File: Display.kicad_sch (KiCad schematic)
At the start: 31 parts, among them J14 LCD_TP_I2C, J15 LCD_SPI, J2 TFT_LCD, U3 MT9284, U5 TPS61169

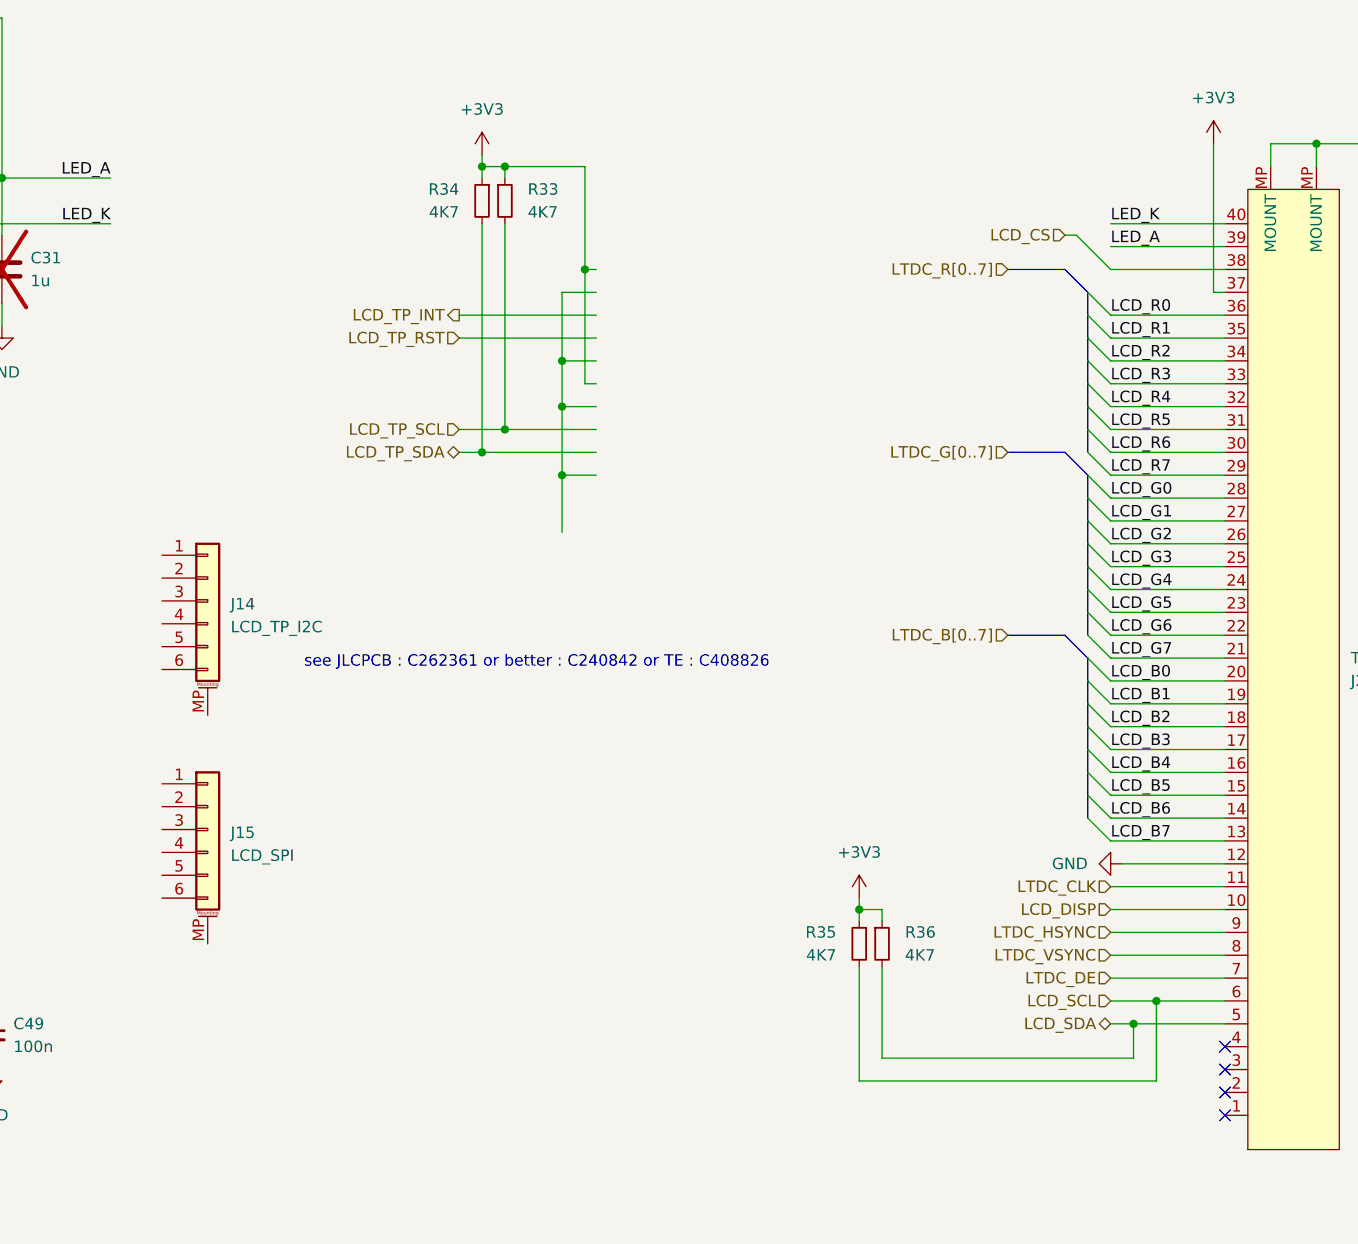
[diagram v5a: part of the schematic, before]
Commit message: Changes: USB C to midmount, CR1220 socket, flip MCU to shorten the LCD traces
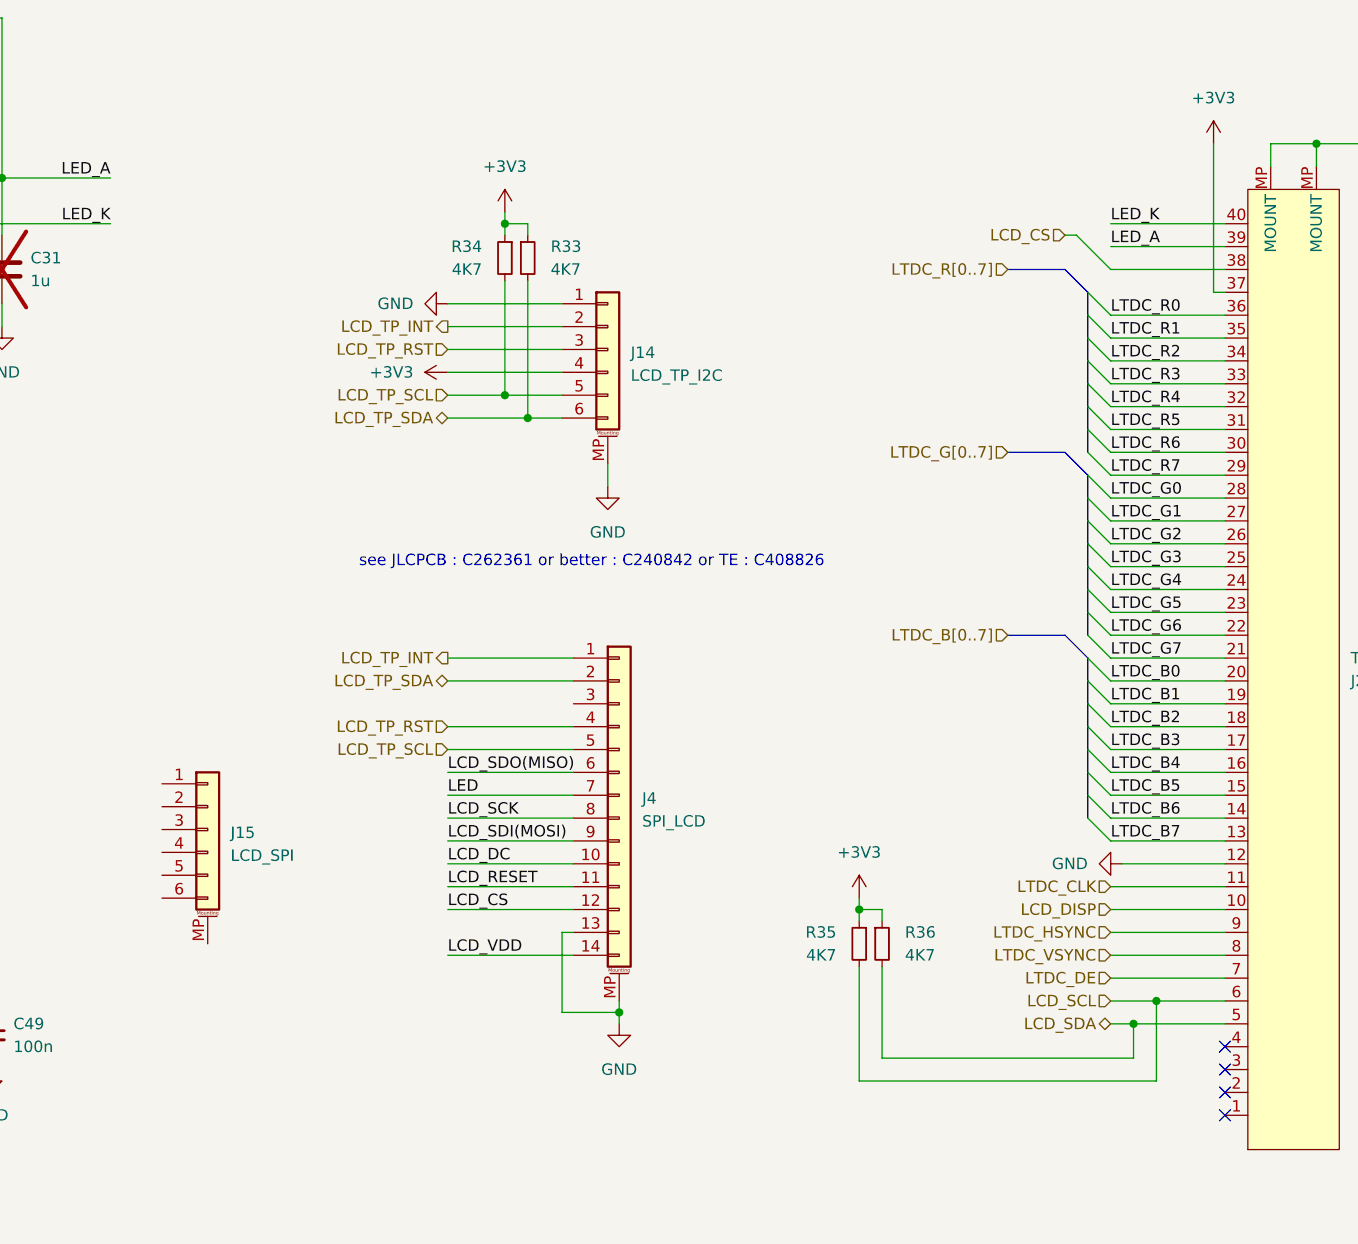
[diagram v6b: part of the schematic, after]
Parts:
- added J4: SPI_LCD, Connector_FFC-FPC:TE_1-84953-4_1x14-1MP_P1.0mm_Horizontal, symbol Connector_Generic_MountingPin:Conn_01x14_MountingPin
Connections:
- net +3V3: now also J14.4 (Pin_4)
- net GND: now also J14.1 (Pin_1), J14.MP (MountPin), J4.13 (Pin_13), J4.MP (MountPin)
- net LCD_CS: now also J4.12 (Pin_12)
- net LCD_TP_INT: now also J14.2 (Pin_2), J4.1 (Pin_1)
- net LCD_TP_RST: now also J14.3 (Pin_3), J4.4 (Pin_4)
- net LCD_TP_SCL: now also J14.5 (Pin_5), R34.2, J4.5 (Pin_5); no longer R33.2
- net LCD_TP_SDA: now also J14.6 (Pin_6), R33.2, J4.2 (Pin_2); no longer R34.2
- net LCD_B0 renamed LTDC_B0
- net LCD_B1 renamed LTDC_B1
- net LCD_B2 renamed LTDC_B2
- net LCD_B3 renamed LTDC_B3
- net LCD_B4 renamed LTDC_B4
- net LCD_B5 renamed LTDC_B5
- net LCD_B6 renamed LTDC_B6
- net LCD_B7 renamed LTDC_B7
- net LCD_G0 renamed LTDC_G0
- net LCD_G1 renamed LTDC_G1
- net LCD_G2 renamed LTDC_G2
- net LCD_G3 renamed LTDC_G3
- net LCD_G4 renamed LTDC_G4
- net LCD_G5 renamed LTDC_G5
- net LCD_G6 renamed LTDC_G6
- net LCD_G7 renamed LTDC_G7
- net LCD_R0 renamed LTDC_R0
- net LCD_R1 renamed LTDC_R1
- net LCD_R2 renamed LTDC_R2
- net LCD_R3 renamed LTDC_R3
- net LCD_R4 renamed LTDC_R4
- net LCD_R5 renamed LTDC_R5
- net LCD_R6 renamed LTDC_R6
- net LCD_R7 renamed LTDC_R7
- new net LCD_DC: J4.10 (Pin_10)
- new net LCD_RESET: J4.11 (Pin_11)
- new net LCD_SCK: J4.8 (Pin_8)
- new net LCD_SDI(MOSI): J4.9 (Pin_9)
- new net LCD_SDO(MISO): J4.6 (Pin_6)
- new net LCD_VDD: J4.14 (Pin_14)
- new net LED: J4.7 (Pin_7)
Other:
- moved on the sheet: J14, R33, R34

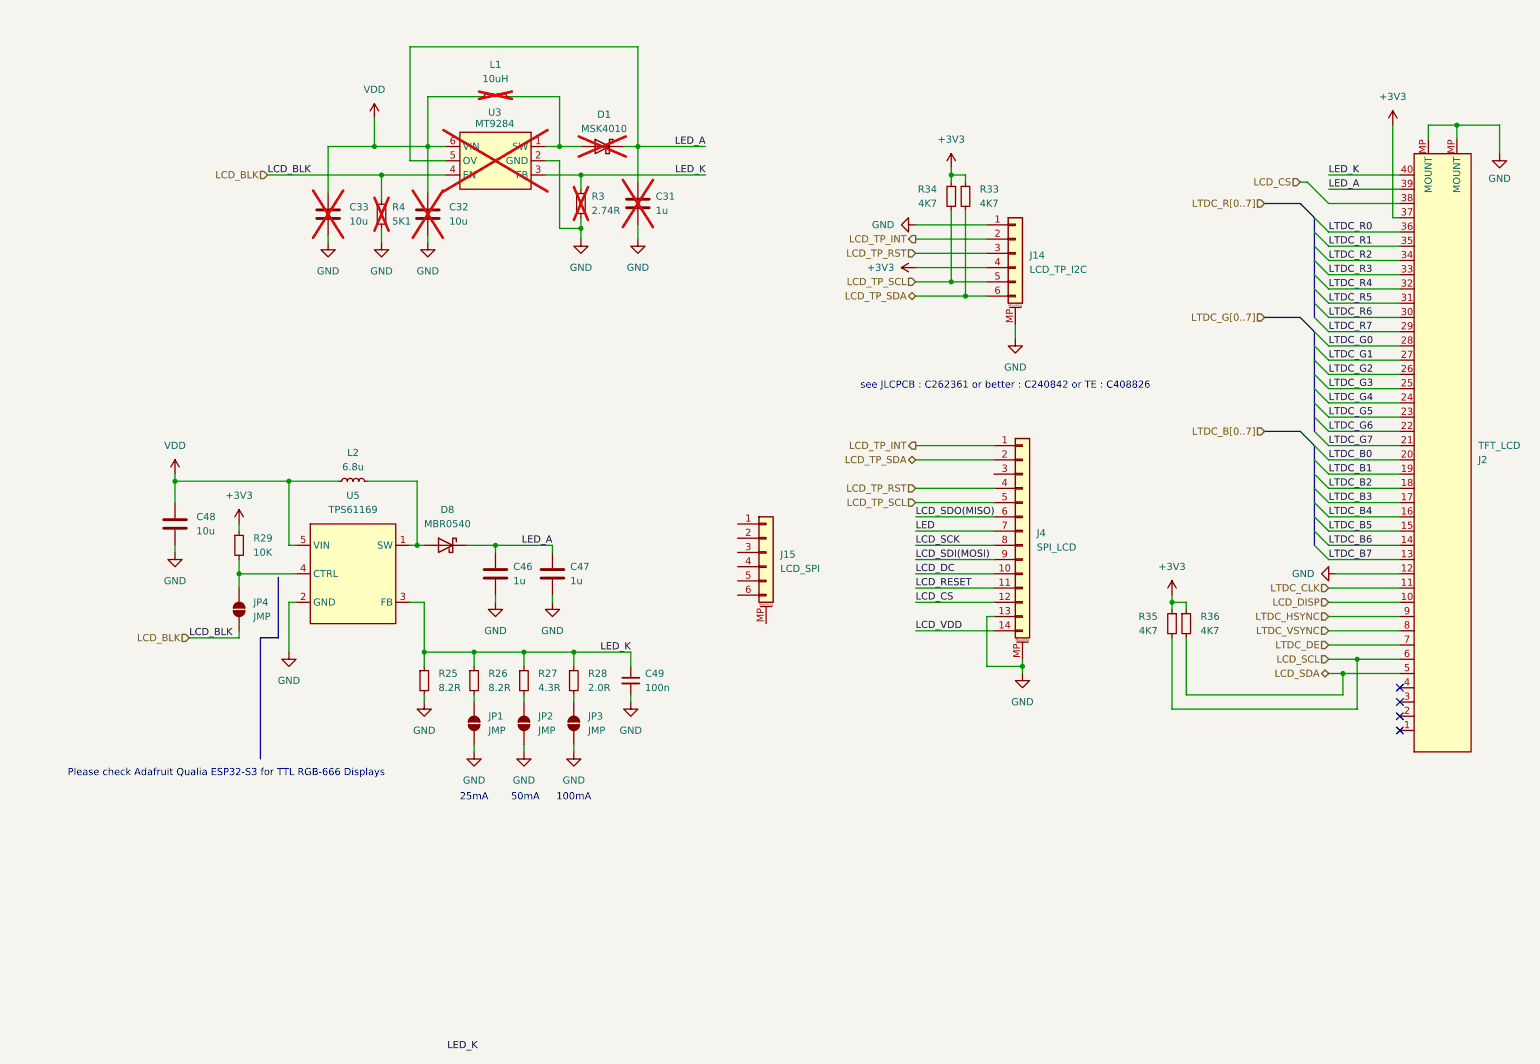
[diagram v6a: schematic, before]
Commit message: Finished SDRAM, LTDC, QSPI, SDMMC, still an error on LTDC B channel
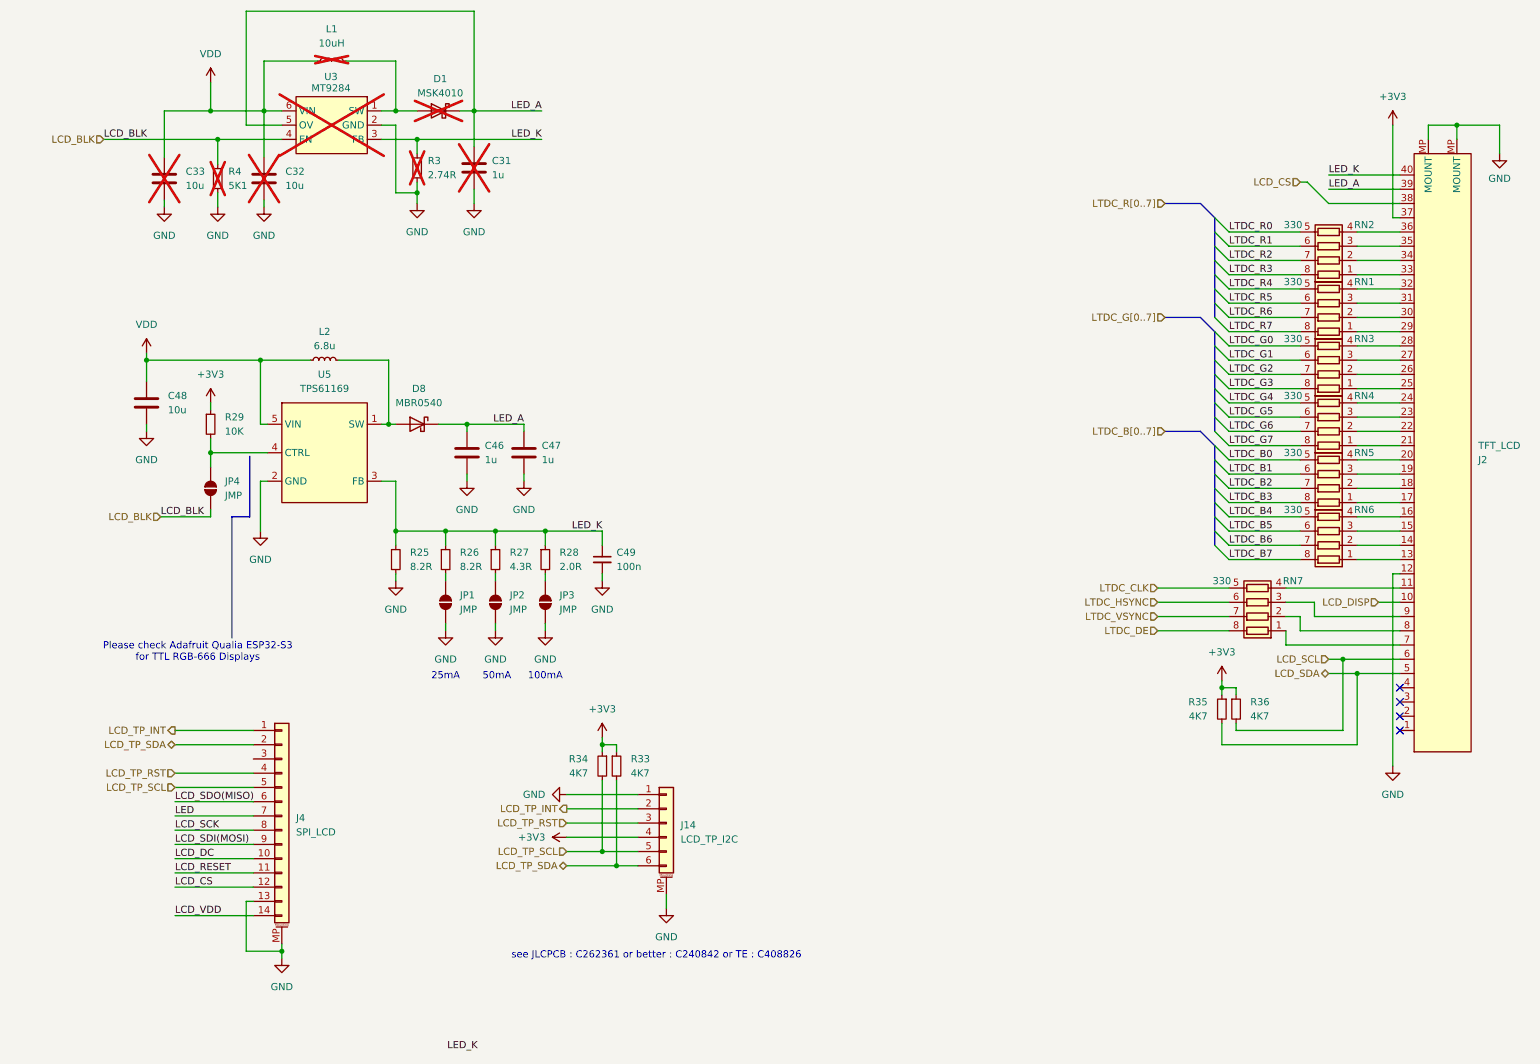
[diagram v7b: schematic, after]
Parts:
- removed J15: LCD_SPI, Connector_FFC-FPC:TE_84952-6_1x06-1MP_P1.0mm_Horizontal, symbol Connector_Generic_MountingPin:Conn_01x06_MountingPin
- added RN1, RN2, RN3, RN4, RN5, RN6, RN7: 330, Resistor_SMD:R_Array_Convex_4x0603, symbol Device:R_Pack04
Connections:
- net LCD_SCL: now also R36.2; no longer R35.2
- net LCD_SDA: now also R35.2; no longer R36.2
- net LTDC_B0: now also RN5.5 (R4.2); no longer J2.20
- net LTDC_B1: now also RN5.6 (R3.2); no longer J2.19
- net LTDC_B2: now also RN5.7 (R2.2); no longer J2.18
- net LTDC_B3: now also RN5.8 (R1.2); no longer J2.17
- net LTDC_B4: now also RN6.5 (R4.2); no longer J2.16
- net LTDC_B5: now also RN6.6 (R3.2); no longer J2.15
- net LTDC_B6: now also RN6.7 (R2.2); no longer J2.14
- net LTDC_B7: now also RN6.8 (R1.2); no longer J2.13
- net LTDC_CLK: now also RN7.5 (R4.2); no longer J2.11
- net LTDC_DE: now also RN7.8 (R1.2); no longer J2.7
- net LTDC_G0: now also RN3.5 (R4.2); no longer J2.28
- net LTDC_G1: now also RN3.6 (R3.2); no longer J2.27
- net LTDC_G2: now also RN3.7 (R2.2); no longer J2.26
- net LTDC_G3: now also RN3.8 (R1.2); no longer J2.25
- net LTDC_G4: now also RN4.5 (R4.2); no longer J2.24
- net LTDC_G5: now also RN4.6 (R3.2); no longer J2.23
- net LTDC_G6: now also RN4.7 (R2.2); no longer J2.22
- net LTDC_G7: now also RN4.8 (R1.2); no longer J2.21
- net LTDC_HSYNC: now also RN7.6 (R3.2); no longer J2.9
- net LTDC_R0: now also RN2.5 (R4.2); no longer J2.36
- net LTDC_R1: now also RN2.6 (R3.2); no longer J2.35
- net LTDC_R2: now also RN2.7 (R2.2); no longer J2.34
- net LTDC_R3: now also RN2.8 (R1.2); no longer J2.33
- net LTDC_R4: now also RN1.5 (R4.2); no longer J2.32
- net LTDC_R5: now also RN1.6 (R3.2); no longer J2.31
- net LTDC_R6: now also RN1.7 (R2.2); no longer J2.30
- net LTDC_R7: now also RN1.8 (R1.2); no longer J2.29
- net LTDC_VSYNC: now also RN7.7 (R2.2); no longer J2.8
- new net: J2.17, RN5.1 (R1.1)
- new net: J2.18, RN5.2 (R2.1)
- new net: J2.19, RN5.3 (R3.1)
- new net: J2.20, RN5.4 (R4.1)
- new net: J2.13, RN6.1 (R1.1)
- new net: J2.14, RN6.2 (R2.1)
- new net: J2.15, RN6.3 (R3.1)
- new net: J2.16, RN6.4 (R4.1)
- new net: J2.25, RN3.1 (R1.1)
- new net: J2.26, RN3.2 (R2.1)
- new net: J2.27, RN3.3 (R3.1)
- new net: J2.28, RN3.4 (R4.1)
- new net: J2.21, RN4.1 (R1.1)
- new net: J2.22, RN4.2 (R2.1)
- new net: J2.23, RN4.3 (R3.1)
- new net: J2.24, RN4.4 (R4.1)
- new net: J2.33, RN2.1 (R1.1)
- new net: J2.34, RN2.2 (R2.1)
- new net: J2.35, RN2.3 (R3.1)
- new net: J2.36, RN2.4 (R4.1)
- new net: J2.29, RN1.1 (R1.1)
- new net: J2.30, RN1.2 (R2.1)
- new net: J2.31, RN1.3 (R3.1)
- new net: J2.32, RN1.4 (R4.1)
- new net: J2.11, RN7.4 (R4.1)
- new net: J2.7, RN7.1 (R1.1)
- new net: J2.8, RN7.2 (R2.1)
- new net: J2.9, RN7.3 (R3.1)
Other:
- moved on the sheet: C31, C32, C33, C46, C47, C48, C49, D1, D8, J14, J4, JP1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

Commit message: Finished SDRAM, QSPI, SDMMC, LTDC, TP, EEPROM, USB, debug (need to verify on UART)
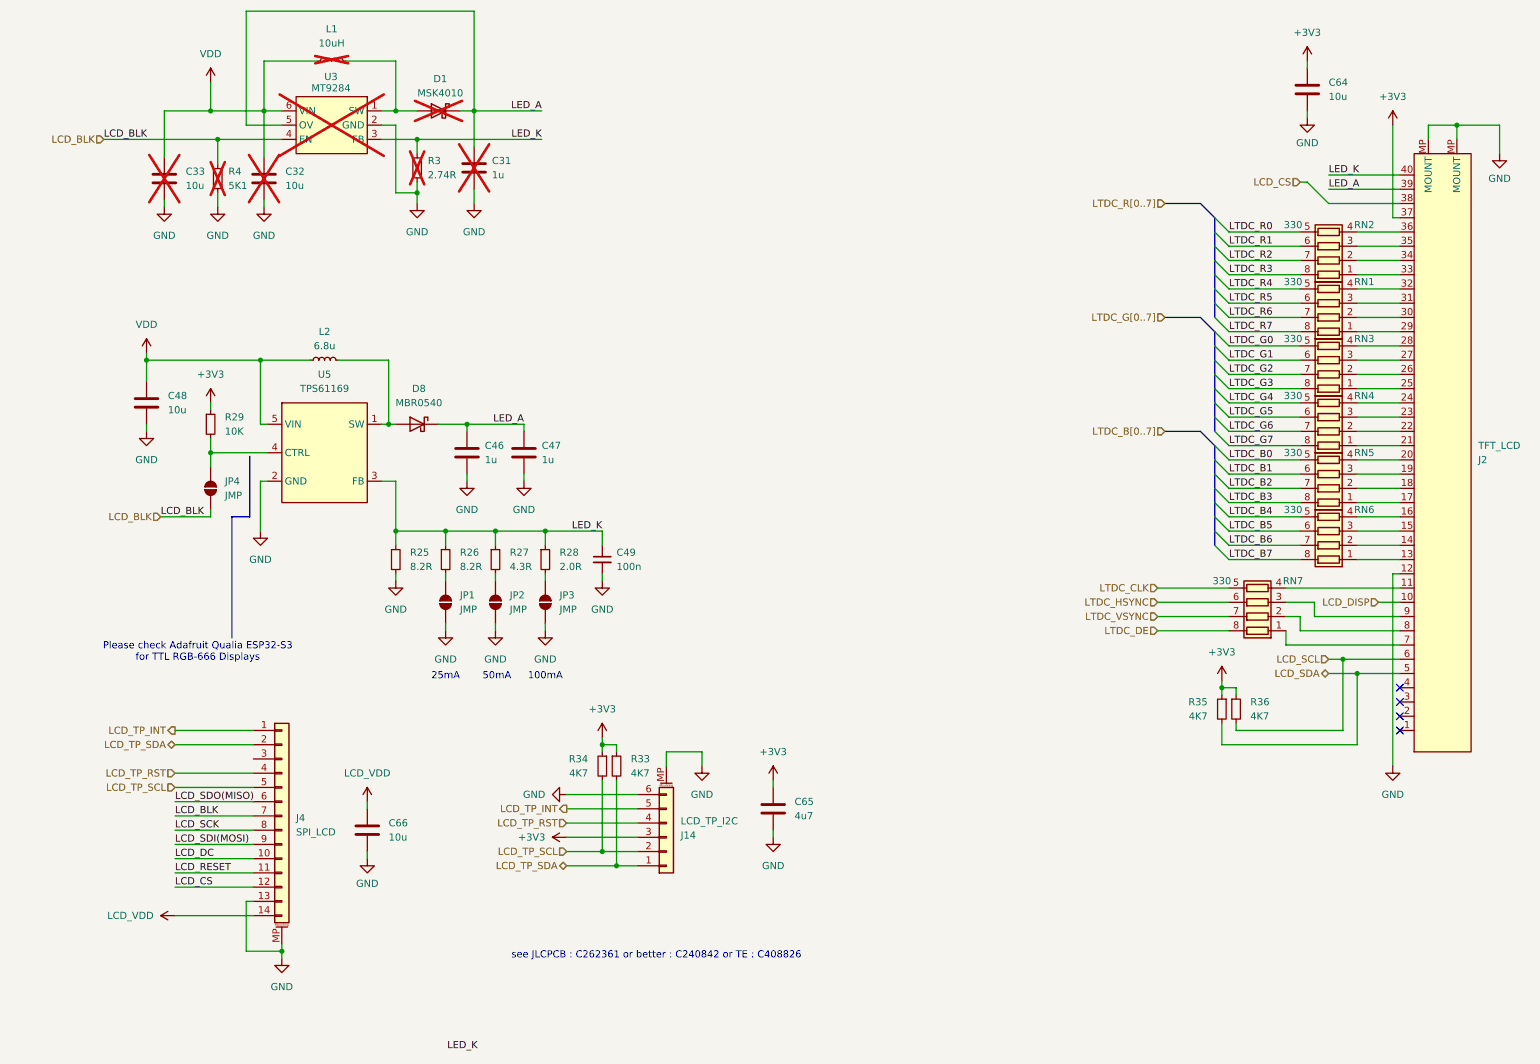
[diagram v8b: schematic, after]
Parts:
- added C64, C66: 10u, Capacitor_SMD:C_0603_1608Metric, symbol Device:C
- added C65: 4u7, Capacitor_SMD:C_0603_1608Metric, symbol Device:C
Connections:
- net LED is gone; now on net LCD_BLK: J4.7 (Pin_7)
- net +3V3: now also J14.3 (Pin_3), C64.1, C65.1; no longer J14.4 (Pin_4)
- net GND: now also J14.6 (Pin_6), C64.2, C65.2, C66.2; no longer J14.1 (Pin_1)
- net LCD_TP_INT: now also J14.5 (Pin_5); no longer J14.2 (Pin_2)
- net LCD_TP_RST: now also J14.4 (Pin_4); no longer J14.3 (Pin_3)
- net LCD_TP_SCL: now also J14.2 (Pin_2); no longer J14.5 (Pin_5)
- net LCD_TP_SDA: now also J14.1 (Pin_1); no longer J14.6 (Pin_6)
- net LCD_VDD: now also C66.1
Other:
- moved on the sheet: J14
